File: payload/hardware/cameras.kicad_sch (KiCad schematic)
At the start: 2 parts

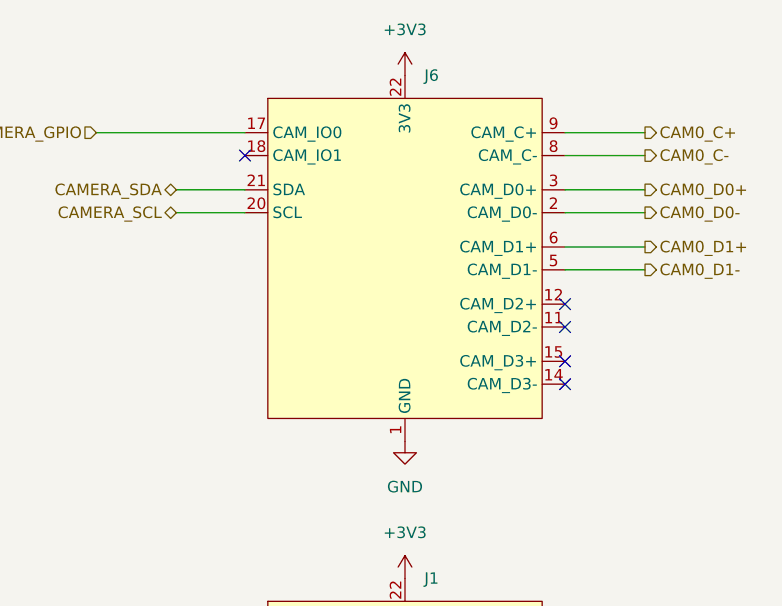
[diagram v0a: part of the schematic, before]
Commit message: add ethernet
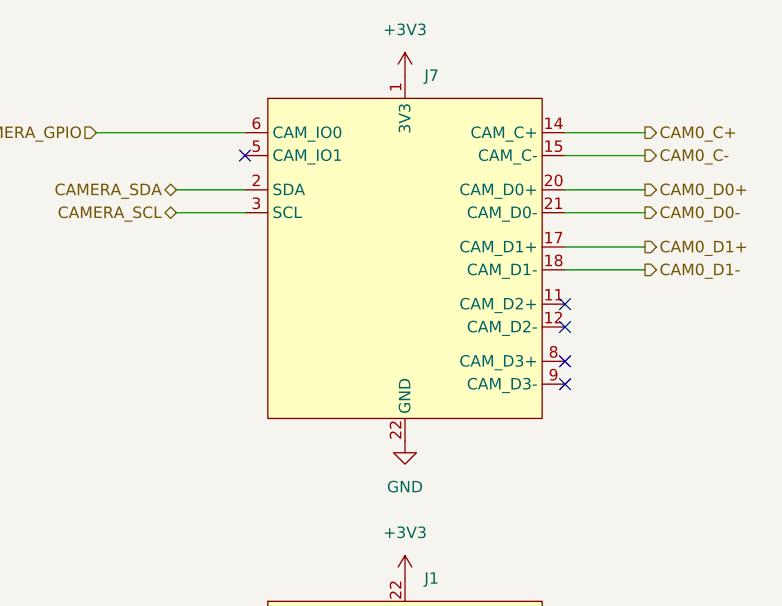
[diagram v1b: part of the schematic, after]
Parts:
- removed J6: (no value), Connector_FFC-FPC:Amphenol_F32Q-1A7x1-11022_1x22-1MP_P0.5mm_Horizontal, symbol payload-syms:Raspberry_Pi_Camera_22_Pin
- added J7: (no value), Connector_FFC-FPC:Amphenol_F32R-1A7x1-11022_1x22-1MP_P0.5mm_Horizontal, symbol payload-syms:Raspberry_Pi_Camera_22_Pin_reversed
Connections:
- net +3V3: now also J7.1 (3V3)
- net CAM0_C+: now also J7.14 (CAM_C+)
- net CAM0_C-: now also J7.15 (CAM_C-)
- net CAM0_D0+: now also J7.20 (CAM_D0+)
- net CAM0_D0-: now also J7.21 (CAM_D0-)
- net CAM0_D1+: now also J7.17 (CAM_D1+)
- net CAM0_D1-: now also J7.18 (CAM_D1-)
- net CAMERA_GPIO: now also J7.6 (CAM_IO0)
- net CAMERA_SCL: now also J7.3 (SCL)
- net CAMERA_SDA: now also J7.2 (SDA)
- net GND: now also J7.10 (GND), J7.13 (GND), J7.16 (GND), J7.19 (GND), J7.22 (GND), J7.4 (GND), J7.7 (GND)
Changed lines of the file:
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@@
+	)
+	(symbol
+		(lib_id "payload-syms:Raspberry_Pi_Camera_22_Pin_reversed")
+		(at 132.08 53.34 0)
+		(unit 1)
+		(body_style 1)
+		(exclude_from_sim no)
+		(in_bom yes)
+		(on_board yes)
+		(in_pos_files yes)
+		(dnp no)
+		(fields_autoplaced yes)
+		(property "Reference" "J7"
+			(at 134.2233 33.02 0)
+			(show_name no)
+			(do_not_autoplace no)
+			(effects
+				(font
+					(size 1.27 1.27)
+				)
+				(justify left)
+			)
+		)
+		(property "Value" ""
+			(at 132.08 53.34 0)
+			(show_name no)
+			(do_not_autoplace no)
+			(effects
+				(font
+					(size 1.27 1.27)
+				)
+			)
+		)
+		(property "Footprint" "Connector_FFC-FPC:Amphenol_F32R-1A7x1-11022_1x22-1MP_P0.5mm_Horizontal"
+			(at 132.08 53.34 0)
+			(hide yes)
+			(show_name no)
+			(do_not_autoplace no)
+			(effects
+				(font
+					(size 1.27 1.27)
+				)
+			)
+		)
+		(property "Datasheet" "https://www.raspberrypi.com/documentation/accessories/camera.html"
+			(at 132.08 53.34 0)
+			(hide yes)
+			(show_name no)
+			(do_not_autoplace no)
+			(effects
+				(font
+					(size 1.27 1.27)
+				)
+			)
+		)
+		(property "Description" "Raspberry pi camera connector, 22 pin, as on the pi zero series and the pi 5, reversed pin order"
+			(at 132.08 53.34 0)
+			(hide yes)
+			(show_name no)
+			(do_not_autoplace no)
+			(effects
+				(font
+					(size 1.27 1.27)
+				)
+			)
+		)
+		(pin "16"
+		)
+		(pin "19"
+		)
+		(pin "21"
+		)
+		(pin "15"
+		)
+		(pin "12"
+		)
+		(pin "5"
+		)
+		(pin "7"
+		)
+		(pin "14"
+		)
+		(pin "13"
+		)
+		(pin "18"
+		)
+		(pin "17"
+		)
+		(pin "8"
+		)
+		(pin "10"
+		)
+		(pin "2"
+		)
+		(pin "4"
+		)
+		(pin "1"
+		)
+		(pin "20"
+		)
+		(pin "11"
+		)
+		(pin "3"
+		)
+		(pin "22"
+		)
+		(pin "9"
+		)
+		(pin "6"
+		)
+		(instances
+			(project "payload"
+				(path "/6c55f0ca-d6e4-4a04-9323-ecf7d8843170/2c1b50ef-7864-4a15-8fab-073a91440387/337d7c74-bd9d-4c92-9640-070bf1fb6685"
+					(reference "J7")
+					(unit 1)
+				)
+			)
+		)
 	)
 	(symbol
@@
 					(unit 1)
 				)
-			)
-		)
-	)
-	(symbol
-		(lib_id "payload-syms:Raspberry_Pi_Camera_22_Pin")
-		(at 132.08 53.34 0)
-		(unit 1)
-		(body_style 1)
-		(exclude_from_sim no)
-		(in_bom yes)
-		(on_board yes)
-		(in_pos_files yes)
-		(dnp no)
-		(fields_autoplaced yes)
-		(property "Reference" "J6"
-			(at 134.2233 33.02 0)
-			(show_name no)
-			(do_not_autoplace no)
-			(effects
-				(font
-					(size 1.27 1.27)
-				)
-				(justify left)
-			)
-		)
-		(property "Value" ""
-			(at 132.08 53.34 0)
-			(show_name no)
-			(do_not_autoplace no)
-			(effects
-				(font
-					(size 1.27 1.27)
-				)
-			)
-		)
-		(property "Footprint" "Connector_FFC-FPC:Amphenol_F32Q-1A7x1-11022_1x22-1MP_P0.5mm_Horizontal"
-			(at 132.08 53.34 0)
-			(hide yes)
-			(show_name no)
-			(do_not_autoplace no)
-			(effects
-				(font
-					(size 1.27 1.27)
-				)
-			)
-		)
-		(property "Datasheet" "https://www.raspberrypi.com/documentation/accessories/camera.html"
-			(at 132.08 53.34 0)
-			(hide yes)
-			(show_name no)
-			(do_not_autoplace no)
-			(effects
-				(font
-					(size 1.27 1.27)
-				)
-			)
-		)
-		(property "Description" "Raspberry pi camera connector, 22 pin, as on the pi zero series and the pi 5"
-			(at 132.08 53.34 0)
-			(hide yes)
-			(show_name no)
-			(do_not_autoplace no)
-			(effects
-				(font
-					(size 1.27 1.27)
-				)
-			)
-		)
-		(property "Availability" ""
-			(at 132.08 53.34 0)
-			(hide yes)
-			(show_name no)
-			(do_not_autoplace no)
-			(effects
-				(font
-					(size 1.27 1.27)
-				)
-			)
-		)
-		(property "Check_prices" ""
-			(at 132.08 53.34 0)
-			(hide yes)
-			(show_name no)
-			(do_not_autoplace no)
-			(effects
-				(font
-					(size 1.27 1.27)
-				)
-			)
-		)
-		(property "Description_1" ""
-			(at 132.08 53.34 0)
-			(hide yes)
-			(show_name no)
-			(do_not_autoplace no)
-			(effects
-				(font
-					(size 1.27 1.27)
-				)
-			)
-		)
-		(property "MANUFACTURER" ""
-			(at 132.08 53.34 0)
-			(hide yes)
-			(show_name no)
-			(do_not_autoplace no)
-			(effects
-				(font
-					(size 1.27 1.27)
-				)
-			)
-		)
-		(property "MANUFACTURER_PART_NUMBER" ""
-			(at 132.08 53.34 0)
-			(hide yes)
-			(show_name no)
-			(do_not_autoplace no)
-			(effects
-				(font
-					(size 1.27 1.27)
-				)
-			)
-		)
-		(property "MAXIMUM_PACKAGE_HEIGHT" ""
-			(at 132.08 53.34 0)
-			(hide yes)
-			(show_name no)
-			(do_not_autoplace no)
-			(effects
-				(font
-					(size 1.27 1.27)
-				)
-			)
-		)
-		(property "MF" ""
-			(at 132.08 53.34 0)
-			(hide yes)
-			(show_name no)
-			(do_not_autoplace no)
-			(effects
-				(font
-					(size 1.27 1.27)
-				)
-			)
-		)
-		(property "MFR_NAME" ""
-			(at 132.08 53.34 0)
-			(hide yes)
-			(show_name no)
-			(do_not_autoplace no)
-			(effects
-				(font
-					(size 1.27 1.27)
-				)
-			)
-		)
-		(property "MP" ""
-			(at 132.08 53.34 0)
-			(hide yes)
-			(show_name no)
-			(do_not_autoplace no)
-			(effects
-				(font
-					(size 1.27 1.27)
-				)
-			)
-		)
-		(property "PARTREV" ""
-			(at 132.08 53.34 0)
-			(hide yes)
-			(show_name no)
-			(do_not_autoplace no)
-			(effects
-				(font
-					(size 1.27 1.27)
-				)
-			)
-		)
-		(property "Package" ""
-			(at 132.08 53.34 0)
-			(hide yes)
-			(show_name no)
-			(do_not_autoplace no)
-			(effects
-				(font
-					(size 1.27 1.27)
-				)
-			)
-		)
-		(property "Price" ""
-			(at 132.08 53.34 0)
-			(hide yes)
-			(show_name no)
-			(do_not_autoplace no)
-			(effects
-				(font
-					(size 1.27 1.27)
-				)
-			)
-		)
-		(property "STANDARD" ""
-			(at 132.08 53.34 0)
-			(hide yes)
-			(show_name no)
-			(do_not_autoplace no)
-			(effects
-				(font
-					(size 1.27 1.27)
-				)
-			)
-		)
-		(property "SnapEDA_Link" ""
-			(at 132.08 53.34 0)
-			(hide yes)
-			(show_name no)
-			(do_not_autoplace no)
-			(effects
-				(font
-					(size 1.27 1.27)
-				)
-			)
-		)
-		(pin "8"
-		)
-		(pin "15"
-		)
-		(pin "13"
-		)
-		(pin "14"
-		)
-		(pin "12"
-		)
-		(pin "7"
-		)
-		(pin "2"
-		)
-		(pin "6"
-		)
-		(pin "16"
-		)
-		(pin "9"
-		)
-		(pin "10"
-		)
-		(pin "11"
-		)
-		(pin "17"
-		)
-		(pin "21"
-		)
-		(pin "18"
-		)
-		(pin "22"
-		)
-		(pin "20"
-		)
-		(pin "4"
-		)
-		(pin "3"
-		)
-		(pin "19"
-		)
-		(pin "1"
-		)
-		(pin "5"
-		)
-		(instances
-			(project "payload"
-				(path "/6c55f0ca-d6e4-4a04-9323-ecf7d8843170/2c1b50ef-7864-4a15-8fab-073a91440387/337d7c74-bd9d-4c92-9640-070bf1fb6685"
-					(reference "J6")
-					(unit 1)
-				)

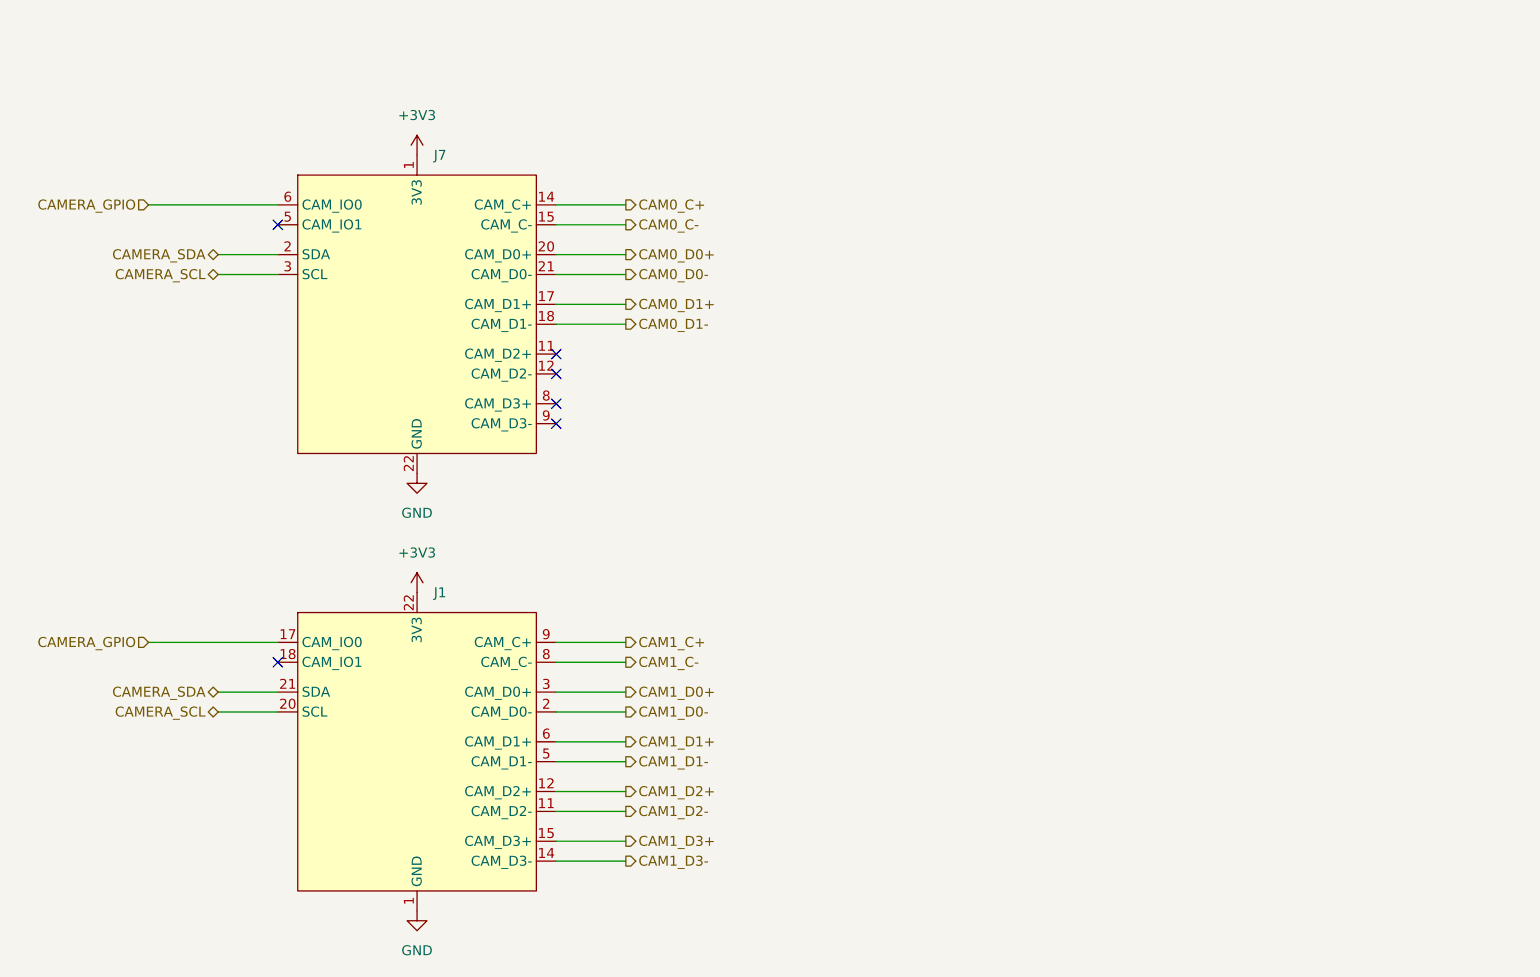
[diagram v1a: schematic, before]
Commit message: add decoupling caps, fix USB skew, add Jax's name
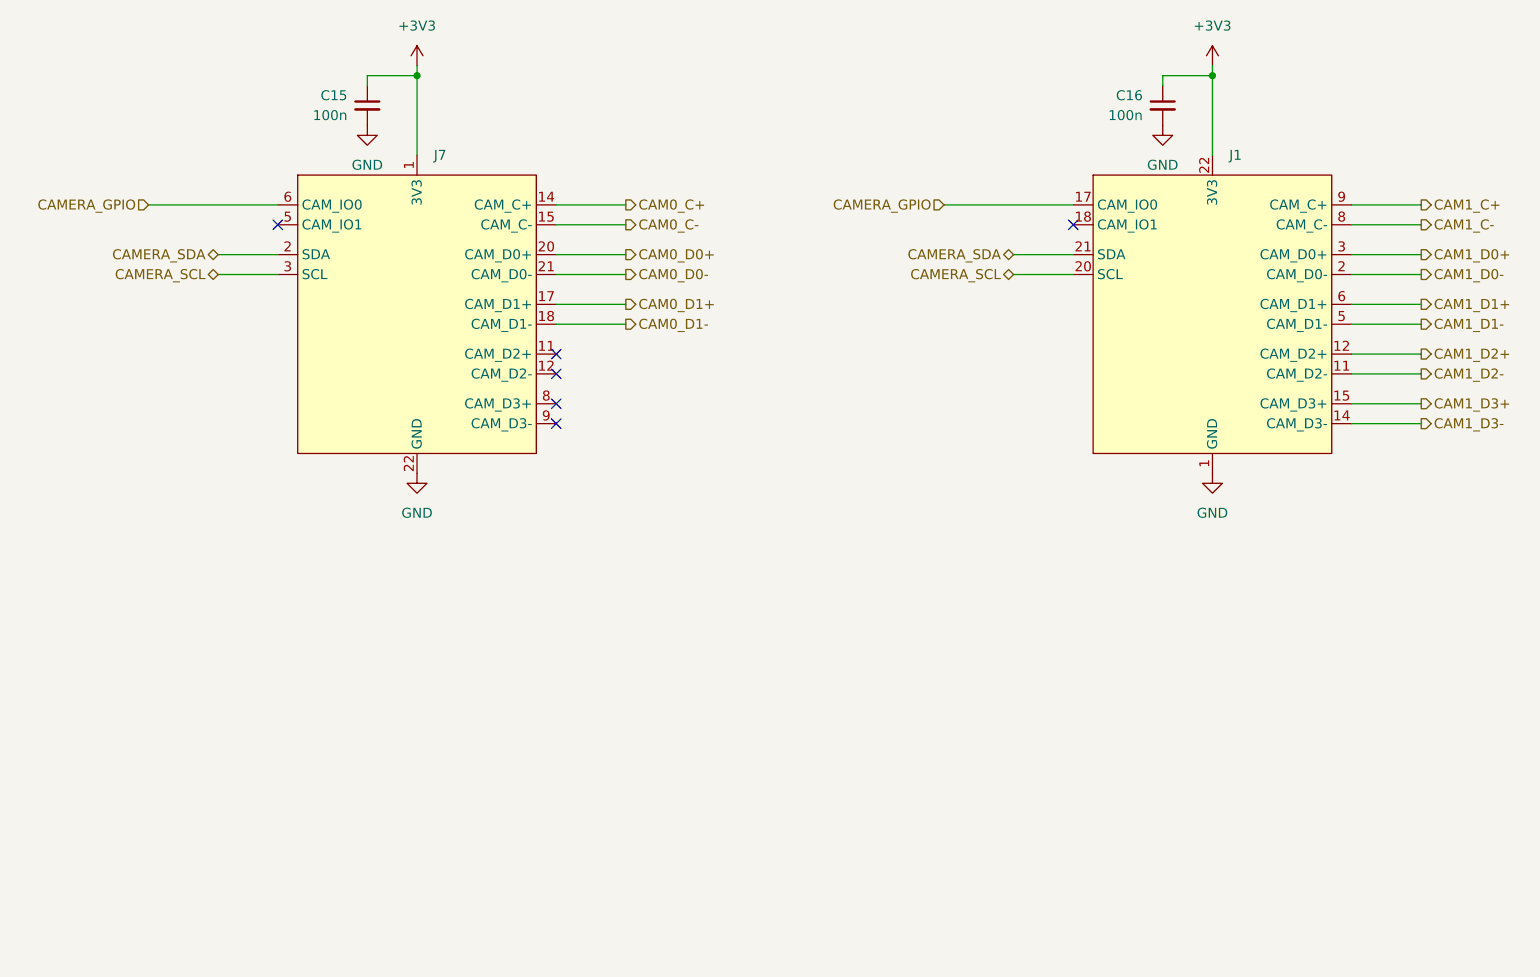
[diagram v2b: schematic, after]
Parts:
- added C15, C16: 100n, Capacitor_SMD:C_0402_1005Metric, symbol Device:C_Small
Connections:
- net +3V3: now also C15.1, C16.1
- net GND: now also C15.2, C16.2
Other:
- moved on the sheet: J1

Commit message: ERC fixes, nits, NC
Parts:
- C15, C16: symbol Device:C_Small -> Device:C_Small_US
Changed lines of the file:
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@@
 	)
 	(symbol
-		(lib_id "Device:C_Small")
+		(lib_id "Device:C_Small_US")
 		(at 125.73 26.67 0)
-		(mirror y)
-		(unit 1)
-		(body_style 1)
-		(exclude_from_sim no)
-		(in_bom yes)
-		(on_board yes)
-		(in_pos_files yes)
-		(dnp no)
-		(fields_autoplaced yes)
+		(unit 1)
+		(body_style 1)
+		(exclude_from_sim no)
+		(in_bom yes)
+		(on_board yes)
+		(in_pos_files yes)
+		(dnp no)
 		(property "Reference" "C15"
-			(at 123.19 25.4062 0)
-			(show_name no)
-			(do_not_autoplace no)
-			(effects
-				(font
-					(size 1.27 1.27)
-				)
-				(justify left)
+			(at 123.19 25.5269 0)
+			(show_name no)
+			(do_not_autoplace no)
+			(effects
+				(font
+					(size 1.27 1.27)
+				)
+				(justify right)
 			)
 		)
 		(property "Value" "100n"
-			(at 123.19 27.9462 0)
-			(show_name no)
-			(do_not_autoplace no)
-			(effects
-				(font
-					(size 1.27 1.27)
-				)
-				(justify left)
+			(at 123.19 28.0669 0)
+			(show_name no)
+			(do_not_autoplace no)
+			(effects
+				(font
+					(size 1.27 1.27)
+				)
+				(justify right)
 			)
 		)
@@
 			)
 		)
-		(property "Description" "Unpolarized capacitor, small symbol"
+		(property "Description" "capacitor, small US symbol"
 			(at 125.73 26.67 0)
 			(hide yes)
@@
 	(symbol
 		(lib_id "power:GND")
+		(at 233.68 73.66 0)
+		(unit 1)
+		(body_style 1)
+		(exclude_from_sim no)
+		(in_bom yes)
+		(on_board yes)
+		(in_pos_files yes)
+		(dnp no)
+		(fields_autoplaced yes)
+		(property "Reference" "#PWR061"
+			(at 233.68 80.01 0)
+			(hide yes)
+			(show_name no)
+			(do_not_autoplace no)
+			(effects
+				(font
+					(size 1.27 1.27)
+				)
+			)
+		)
+		(property "Value" "GND"
+			(at 233.68 78.74 0)
+			(show_name no)
+			(do_not_autoplace no)
+			(effects
+				(font
+					(size 1.27 1.27)
+				)
+			)
+		)
+		(property "Footprint" ""
+			(at 233.68 73.66 0)
+			(hide yes)
+			(show_name no)
+			(do_not_autoplace no)
+			(effects
+				(font
+					(size 1.27 1.27)
+				)
+			)
+		)
+		(property "Datasheet" ""
+			(at 233.68 73.66 0)
+			(hide yes)
+			(show_name no)
+			(do_not_autoplace no)
+			(effects
+				(font
+					(size 1.27 1.27)
+				)
+			)
+		)
+		(property "Description" "Power symbol creates a global label with name \"GND\" , ground"
+			(at 233.68 73.66 0)
+			(hide yes)
+			(show_name no)
+			(do_not_autoplace no)
+			(effects
+				(font
+					(size 1.27 1.27)
+				)
+			)
+		)
+		(pin "1"
+		)
+		(instances
+			(project "payload"
+				(path "/6c55f0ca-d6e4-4a04-9323-ecf7d8843170/2c1b50ef-7864-4a15-8fab-073a91440387/337d7c74-bd9d-4c92-9640-070bf1fb6685"
+					(reference "#PWR061")
+					(unit 1)
+				)
+			)
+		)
+	)
+	(symbol
+		(lib_id "power:GND")
 		(at 227.33 29.21 0)
 		(mirror y)
@@
 	)
 	(symbol
-		(lib_id "power:GND")
-		(at 233.68 73.66 0)
-		(unit 1)
-		(body_style 1)
-		(exclude_from_sim no)
-		(in_bom yes)
-		(on_board yes)
-		(in_pos_files yes)
-		(dnp no)
-		(fields_autoplaced yes)
-		(property "Reference" "#PWR08"
-			(at 233.68 80.01 0)
-			(hide yes)
-			(show_name no)
-			(do_not_autoplace no)
-			(effects
-				(font
-					(size 1.27 1.27)
-				)
-			)
-		)
-		(property "Value" "GND"
-			(at 233.68 78.74 0)
-			(show_name no)
-			(do_not_autoplace no)
-			(effects
-				(font
-					(size 1.27 1.27)
-				)
-			)
-		)
-		(property "Footprint" ""
-			(at 233.68 73.66 0)
-			(hide yes)
-			(show_name no)
-			(do_not_autoplace no)
-			(effects
-				(font
-					(size 1.27 1.27)
-				)
-			)
-		)
-		(property "Datasheet" ""
-			(at 233.68 73.66 0)
-			(hide yes)
-			(show_name no)
-			(do_not_autoplace no)
-			(effects
-				(font
-					(size 1.27 1.27)
-				)
-			)
-		)
-		(property "Description" "Power symbol creates a global label with name \"GND\" , ground"
-			(at 233.68 73.66 0)
-			(hide yes)
-			(show_name no)
-			(do_not_autoplace no)
-			(effects
-				(font
-					(size 1.27 1.27)
-				)
-			)
-		)
-		(pin "1"
-		)
-		(instances
-			(project "payload"
-				(path "/6c55f0ca-d6e4-4a04-9323-ecf7d8843170/2c1b50ef-7864-4a15-8fab-073a91440387/337d7c74-bd9d-4c92-9640-070bf1fb6685"
-					(reference "#PWR08")
-					(unit 1)
-				)
-			)
-		)
-	)
-	(symbol
-		(lib_id "Device:C_Small")
+		(lib_id "Device:C_Small_US")
 		(at 227.33 26.67 0)
-		(mirror y)
-		(unit 1)
-		(body_style 1)
-		(exclude_from_sim no)
-		(in_bom yes)
-		(on_board yes)
-		(in_pos_files yes)
-		(dnp no)
-		(fields_autoplaced yes)
+		(unit 1)
+		(body_style 1)
+		(exclude_from_sim no)
+		(in_bom yes)
+		(on_board yes)
+		(in_pos_files yes)
+		(dnp no)
 		(property "Reference" "C16"
-			(at 224.79 25.4062 0)
-			(show_name no)
-			(do_not_autoplace no)
-			(effects
-				(font
-					(size 1.27 1.27)
-				)
-				(justify left)
+			(at 224.79 25.5269 0)
+			(show_name no)
+			(do_not_autoplace no)
+			(effects
+				(font
+					(size 1.27 1.27)
+				)
+				(justify right)
 			)
 		)
 		(property "Value" "100n"
-			(at 224.79 27.9462 0)
-			(show_name no)
-			(do_not_autoplace no)
-			(effects
-				(font
-					(size 1.27 1.27)
-				)
-				(justify left)
+			(at 224.79 28.0669 0)
+			(show_name no)
+			(do_not_autoplace no)
+			(effects
+				(font
+					(size 1.27 1.27)
+				)
+				(justify right)
 			)
 		)
@@
 			)
 		)
-		(property "Description" "Unpolarized capacitor, small symbol"
+		(property "Description" "capacitor, small US symbol"
 			(at 227.33 26.67 0)
 			(hide yes)

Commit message: add digikey part numbers
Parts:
- C15, C16: Digikey (none) -> 1276-1001-1-ND
- J1: Digikey (none) -> 609-F32Q-1A7H1-11022CT-ND
- J7: Digikey (none) -> 609-F32R-1A7H1-11022CT-ND
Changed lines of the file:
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@@
+			)
+		)
+		(property "Digikey" "609-F32Q-1A7H1-11022CT-ND"
+			(at 233.68 53.34 0)
+			(hide yes)
+			(show_name no)
+			(do_not_autoplace no)
+			(effects
+				(font
+					(size 1.27 1.27)
+				)
 			)
 		)
@@
 			)
 		)
+		(property "Digikey" "1276-1001-1-ND"
+			(at 125.73 26.67 0)
+			(hide yes)
+			(show_name no)
+			(do_not_autoplace no)
+			(effects
+				(font
+					(size 1.27 1.27)
+				)
+			)
+		)
 		(pin "2"
 		)
@@
 			)
 		)
+		(property "Digikey" "609-F32R-1A7H1-11022CT-ND"
+			(at 132.08 53.34 0)
+			(hide yes)
+			(show_name no)
+			(do_not_autoplace no)
+			(effects
+				(font
+					(size 1.27 1.27)
+				)
+			)
+		)
 		(pin "16"
 		)
@@
 			(at 227.33 26.67 0)
 			(hide yes)
+			(show_name no)
+			(do_not_autoplace no)
+			(effects
+				(font
+					(size 1.27 1.27)
+				)
+			)
+		)
+		(property "Digikey" "1276-1001-1-ND"
+			(at 227.33 26.67 0)
+			(hide yes)
